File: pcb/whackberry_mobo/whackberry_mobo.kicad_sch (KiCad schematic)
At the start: 1 part

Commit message: more kicad work
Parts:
- added D1: LD271, LED_THT:LED_D5.0mm_IRGrey, symbol LED:LD271
- added S1: 5WayNav_504, Whackberry_Parts_Library:5WayNav_504, symbol Whackberry_Symbols_Library:5WayNav_504
- added U2: TSOP348xx, OptoDevice:Vishay_MOLD-3Pin, symbol Interface_Optical:TSOP348xx
- added U3: ~, Whackberry_Parts_Library:QT_Py, symbol Whackberry_Symbols_Library:QTPy
- added U4: ~, Whackberry_Parts_Library:Camera, symbol Whackberry_Symbols_Library:Camera
- added U5: 2232_display, Whackberry_Parts_Library:Display_MODULE_2232, symbol Whackberry_Symbols_Library:2232_display

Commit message: another kicad work save
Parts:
- added R1: R, symbol Device:R
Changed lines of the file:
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@@
 	(paper "A4")
+	(symbol
+		(lib_id "Device:R")
+		(at 139.7 85.09 0)
+		(unit 1)
+		(exclude_from_sim no)
+		(in_bom yes)
+		(on_board yes)
+		(dnp no)
+		(fields_autoplaced yes)
+		(property "Reference" "R1"
+			(at 142.24 83.8199 0)
+			(effects
+				(font
+					(size 1.27 1.27)
+				)
+				(justify left)
+			)
+		)
+		(property "Value" "R"
+			(at 142.24 86.3599 0)
+			(effects
+				(font
+					(size 1.27 1.27)
+				)
+				(justify left)
+			)
+		)
+		(property "Footprint" ""
+			(at 137.922 85.09 90)
+			(effects
+				(font
+					(size 1.27 1.27)
+				)
+				(hide yes)
+			)
+		)
+		(property "Datasheet" "~"
+			(at 139.7 85.09 0)
+			(effects
+				(font
+					(size 1.27 1.27)
+				)
+				(hide yes)
+			)
+		)
+		(property "Description" "Resistor"
+			(at 139.7 85.09 0)
+			(effects
+				(font
+					(size 1.27 1.27)
+				)
+				(hide yes)
+			)
+		)
+		(pin "1"
+		)
+		(pin "2"
+		)
+		(instances
+			(project ""
+				(path "/efde2cb3-16ef-4cc9-81c7-d9f2adf33283"
+					(reference "R1")
+					(unit 1)
+				)
+			)
+		)
+	)
 	(symbol
 		(lib_id "Whackberry_Symbols_Library:Camera")

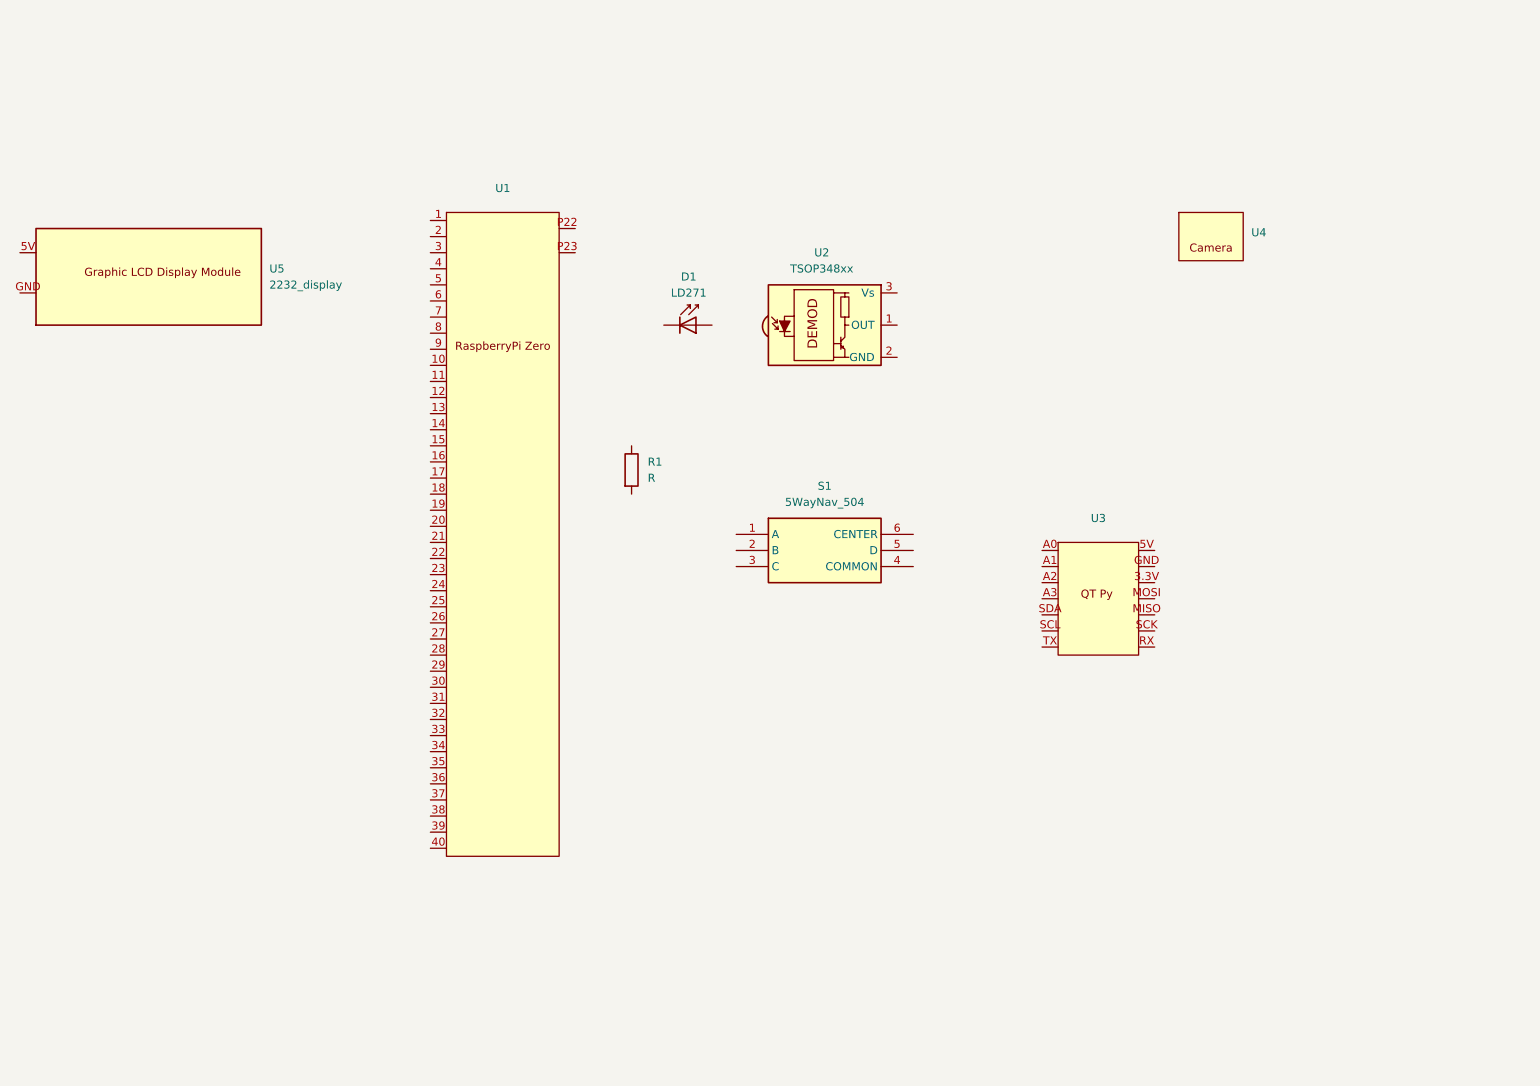
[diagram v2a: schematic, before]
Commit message: adding last batch of symbols and footprints in KiCad
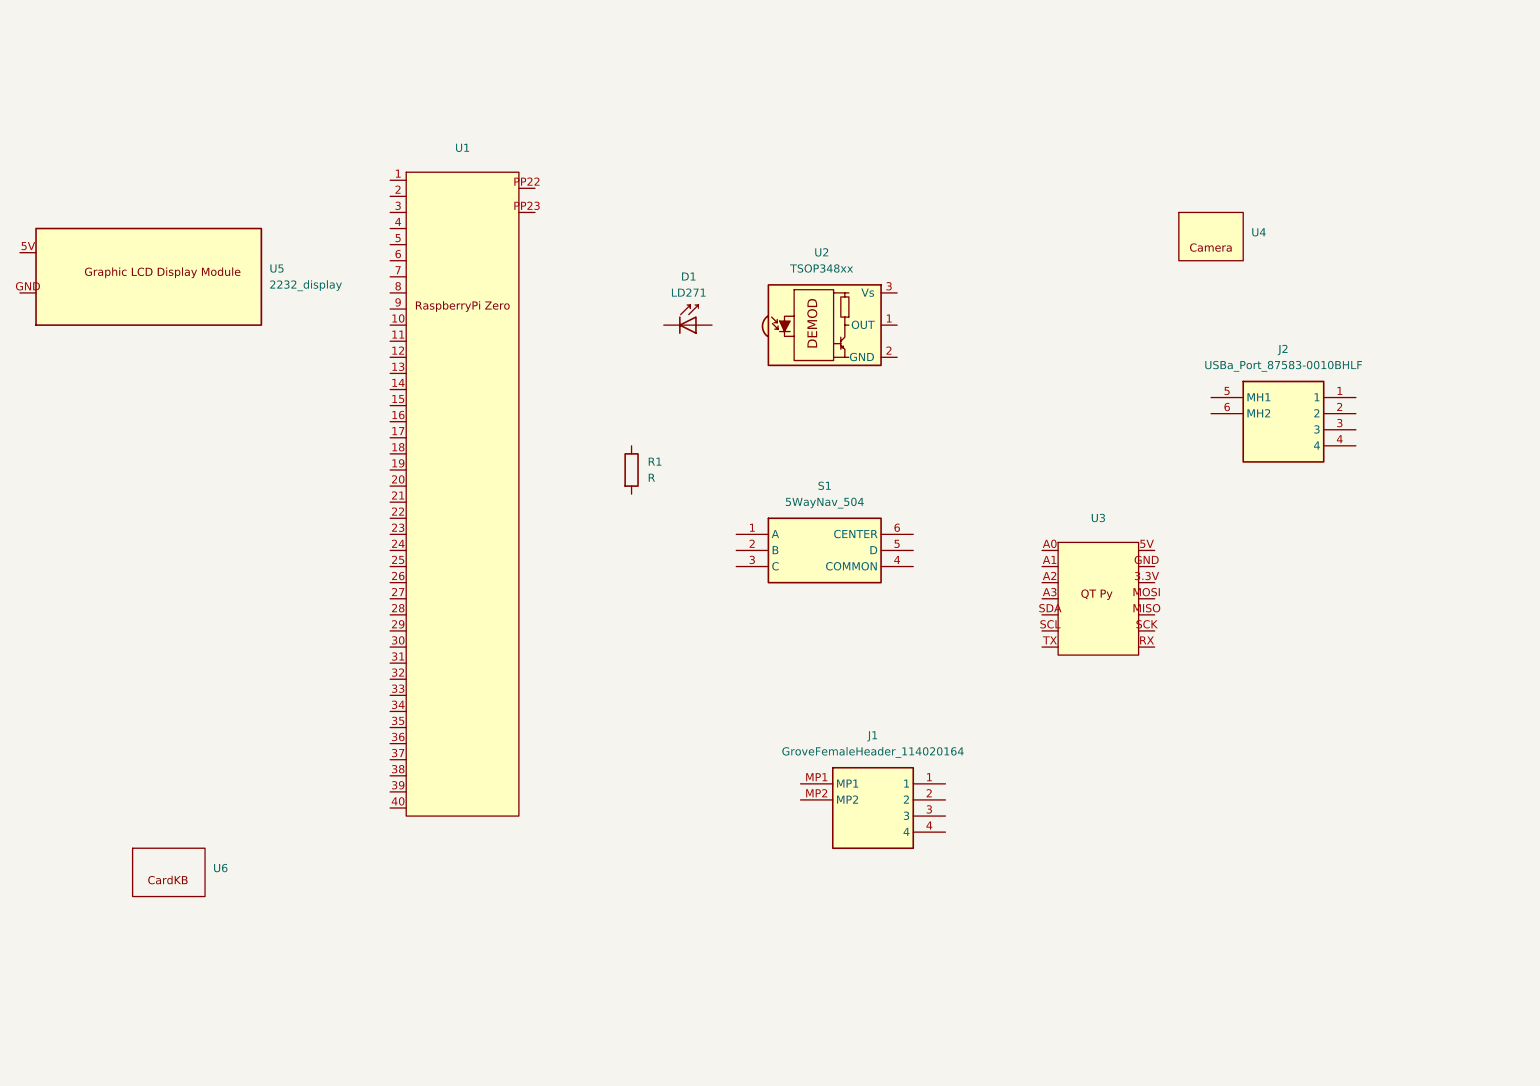
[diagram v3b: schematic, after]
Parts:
- added J1: GroveFemaleHeader_114020164, Whackberry_Parts_Library:GroveFemaleHeader_114020164, symbol Whackberry_Symbols_Library:GroveFemaleHeader_114020164
- added J2: USBa_Port_87583-0010BHLF, Whackberry_Parts_Library:USBa_Port_875830010BHLF, symbol Whackberry_Symbols_Library:USBa_Port_87583-0010BHLF
- added U6: ~, Whackberry_Parts_Library:CardKB, symbol Whackberry_Symbols_Library:KardKB

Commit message: placing parts on PCB
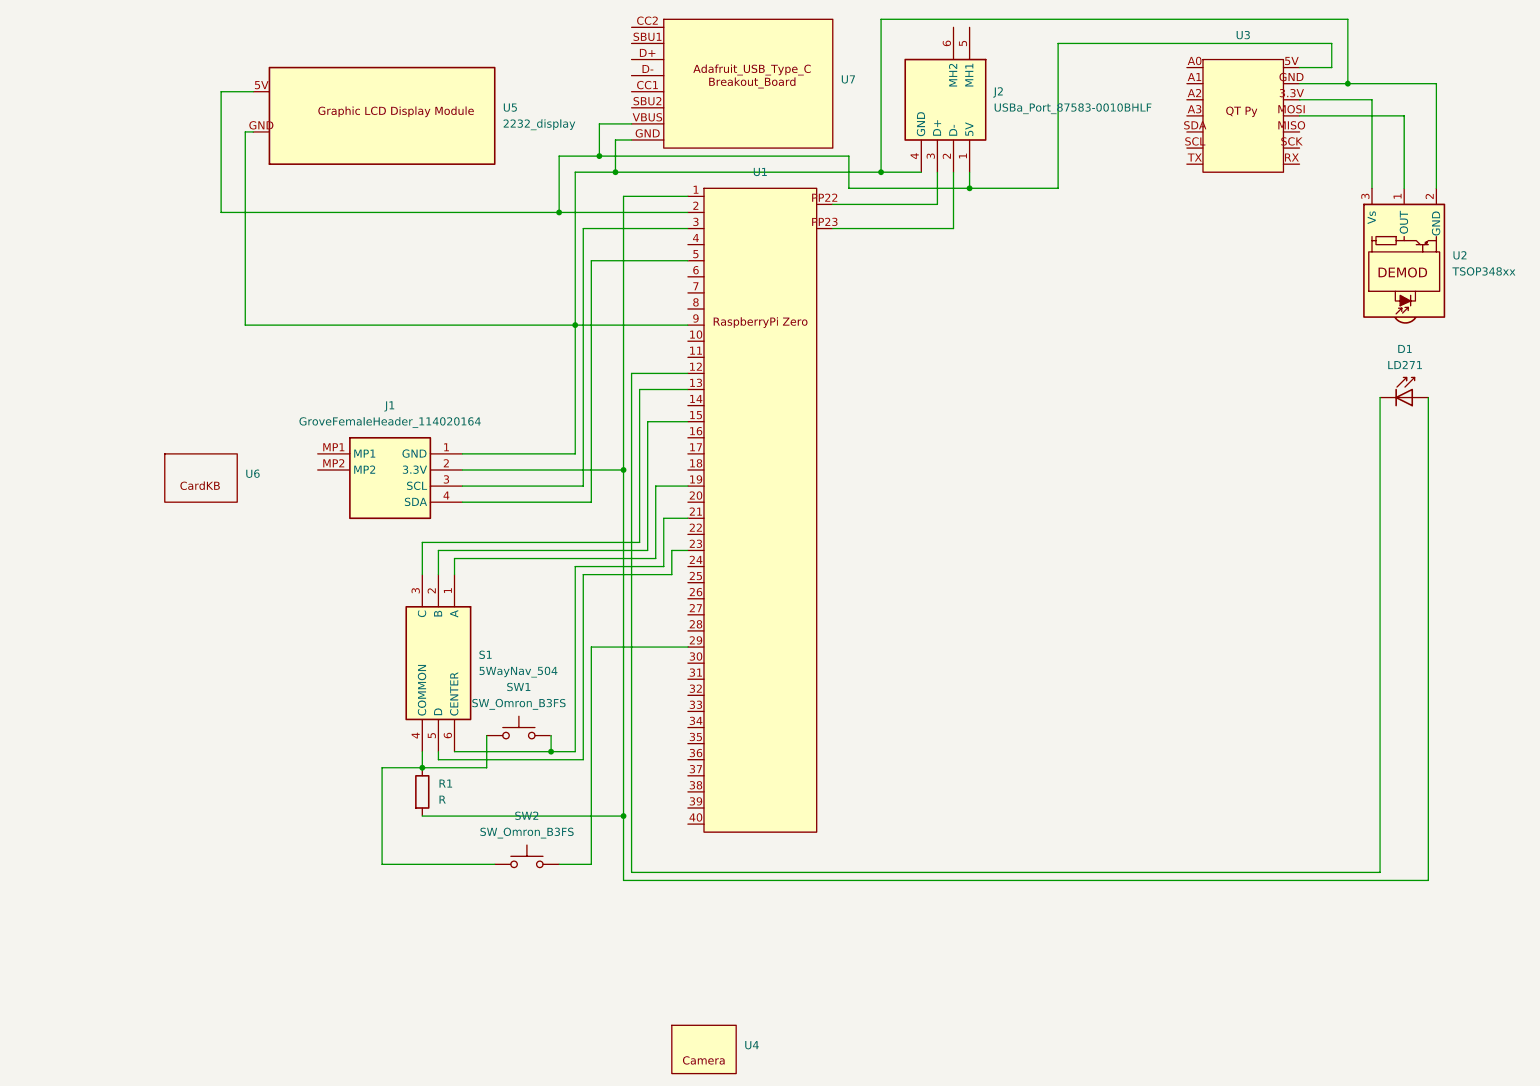
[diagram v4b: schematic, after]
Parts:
- added SW1, SW2: SW_Omron_B3FS, Button_Switch_THT:SW_TH_Tactile_Omron_B3F-10xx, symbol Switch:SW_Omron_B3FS
- added U7: ~, Whackberry_Parts_Library:Adafruit_USB_Type_C_Breakout_Board, symbol Whackberry_Symbols_Library:Adafruit_USB_Type_C_Breakout_Board
- R1: footprint (none) -> Resistor_THT:R_Axial_DIN0207_L6.3mm_D2.5mm_P10.16mm_Horizontal
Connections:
- net at R1.1: now also S1.4 (COMMON), SW1.1, SW2.1
- net at R1.2: now also D1.2 (A), J1.2 (3.3V), U1.1
- net at J2.1 (5V): now also U1.2, U3.5V, U5.5V, U7.VBUS
- net at J2.2 (D-): now also U1.PP23
- net at J2.3 (D+): now also U1.PP22
- net at J2.4 (GND): now also J1.1 (GND), U1.9, U2.2 (GND), U3.GND, U5.GND, U7.GND
- net at D1.1 (K): now also U1.12
- net at U1.13: now also S1.3 (C)
- net at U1.15: now also S1.2 (B)
- net at U1.19: now also S1.1 (A)
- net at U1.21: now also S1.6 (CENTER), SW1.2
- net at U1.23: now also S1.5 (D)
- net at U1.29: now also SW2.2
- net at U1.3: now also J1.3 (SCL)
- net at U1.5: now also J1.4 (SDA)
- net at U2.1 (OUT): now also U3.MOSI
- net at U2.3 (Vs): now also U3.3.3V
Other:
- moved on the sheet: D1, R1, S1, U1, U2, U3, U4, U5, U6

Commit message: Ready for tracing PCB
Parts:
- renumbered S1 to 5WayNav-1, U6 to CardKB-1, J1 to GROVE-1, D1 to IR-LED-1, U2 to IR-Re-1, U5 to LCD-1, U3 to QTpy-1, U1 to RPi-Zero-1, J2 to USB-A-1, U7 to USB-C-1
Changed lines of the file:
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@@
 		(dnp no)
 		(fields_autoplaced yes)
-		(property "Reference" "J2"
+		(property "Reference" "USB-A-1"
 			(at 196.85 25.3999 90)
 			(effects
@@
 			(project ""
 				(path "/efde2cb3-16ef-4cc9-81c7-d9f2adf33283"
-					(reference "J2")
+					(reference "USB-A-1")
 					(unit 1)
 				)
@@
 		(dnp no)
 		(fields_autoplaced yes)
-		(property "Reference" "D1"
+		(property "Reference" "IR-LED-1"
 			(at 261.747 66.04 0)
 			(effects
@@
 			(project ""
 				(path "/efde2cb3-16ef-4cc9-81c7-d9f2adf33283"
-					(reference "D1")
+					(reference "IR-LED-1")
 					(unit 1)
 				)
@@
 		(dnp no)
 		(fields_autoplaced yes)
-		(property "Reference" "U1"
+		(property "Reference" "RPi-Zero-1"
 			(at 160.02 38.1 0)
 			(effects
@@
 			(project ""
 				(path "/efde2cb3-16ef-4cc9-81c7-d9f2adf33283"
-					(reference "U1")
+					(reference "RPi-Zero-1")
 					(unit 1)
 				)
@@
 		(dnp no)
 		(fields_autoplaced yes)
-		(property "Reference" "U6"
+		(property "Reference" "CardKB-1"
 			(at 78.74 85.7249 0)
 			(effects
@@
 			(project ""
 				(path "/efde2cb3-16ef-4cc9-81c7-d9f2adf33283"
-					(reference "U6")
+					(reference "CardKB-1")
 					(unit 1)
 				)
@@
 		(dnp no)
 		(fields_autoplaced yes)
-		(property "Reference" "U2"
+		(property "Reference" "IR-Re-1"
 			(at 269.24 51.2648 90)
 			(effects
@@
 			(project ""
 				(path "/efde2cb3-16ef-4cc9-81c7-d9f2adf33283"
-					(reference "U2")
+					(reference "IR-Re-1")
 					(unit 1)
 				)
@@
 		(dnp no)
 		(fields_autoplaced yes)
-		(property "Reference" "U3"
+		(property "Reference" "QTpy-1"
 			(at 236.22 16.51 0)
 			(effects
@@
 			(project ""
 				(path "/efde2cb3-16ef-4cc9-81c7-d9f2adf33283"
-					(reference "U3")
+					(reference "QTpy-1")
 					(unit 1)
 				)
@@
 		(dnp no)
 		(fields_autoplaced yes)
-		(property "Reference" "J1"
+		(property "Reference" "GROVE-1"
 			(at 101.6 74.93 0)
 			(effects
@@
 			(project ""
 				(path "/efde2cb3-16ef-4cc9-81c7-d9f2adf33283"
-					(reference "J1")
+					(reference "GROVE-1")
 					(unit 1)
 				)
@@
 		(dnp no)
 		(fields_autoplaced yes)
-		(property "Reference" "U7"
+		(property "Reference" "USB-C-1"
 			(at 172.72 23.4949 0)
 			(effects
@@
 			(project ""
 				(path "/efde2cb3-16ef-4cc9-81c7-d9f2adf33283"
-					(reference "U7")
+					(reference "USB-C-1")
 					(unit 1)
 				)
@@
 		(dnp no)
 		(fields_autoplaced yes)
-		(property "Reference" "S1"
+		(property "Reference" "5WayNav-1"
 			(at 115.57 114.2999 90)
 			(effects
@@
 			(project ""
 				(path "/efde2cb3-16ef-4cc9-81c7-d9f2adf33283"
-					(reference "S1")
+					(reference "5WayNav-1")
 					(unit 1)
 				)
@@
 		(dnp no)
 		(fields_autoplaced yes)
-		(property "Reference" "U5"
+		(property "Reference" "LCD-1"
 			(at 119.38 27.9399 0)
 			(effects
@@
 			(project ""
 				(path "/efde2cb3-16ef-4cc9-81c7-d9f2adf33283"
-					(reference "U5")
+					(reference "LCD-1")
 					(unit 1)
 				)
